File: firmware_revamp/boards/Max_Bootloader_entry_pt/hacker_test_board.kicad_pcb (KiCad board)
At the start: 2 copper layers, 109.3 x 58.3 mm, 19 parts, among them U101 TPS560430YF

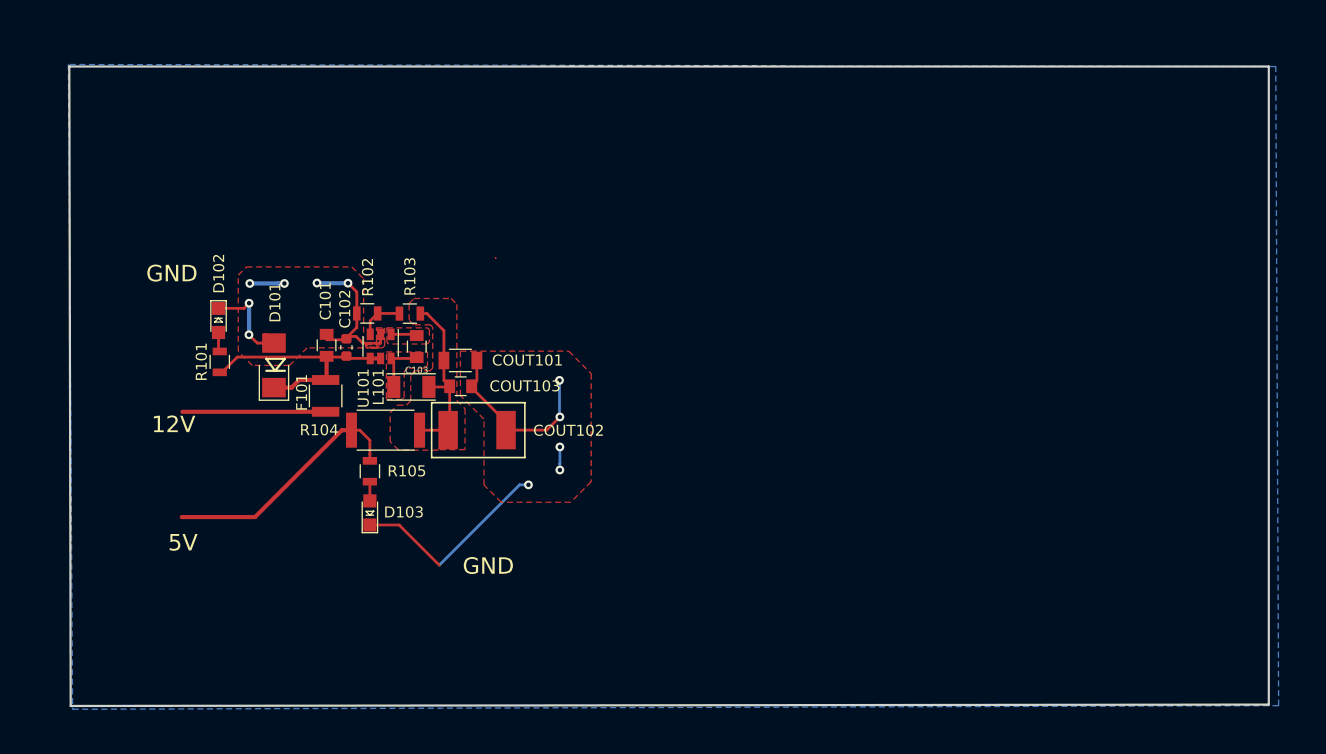
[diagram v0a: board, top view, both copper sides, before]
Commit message: Completed first layout draft of Bootloader board
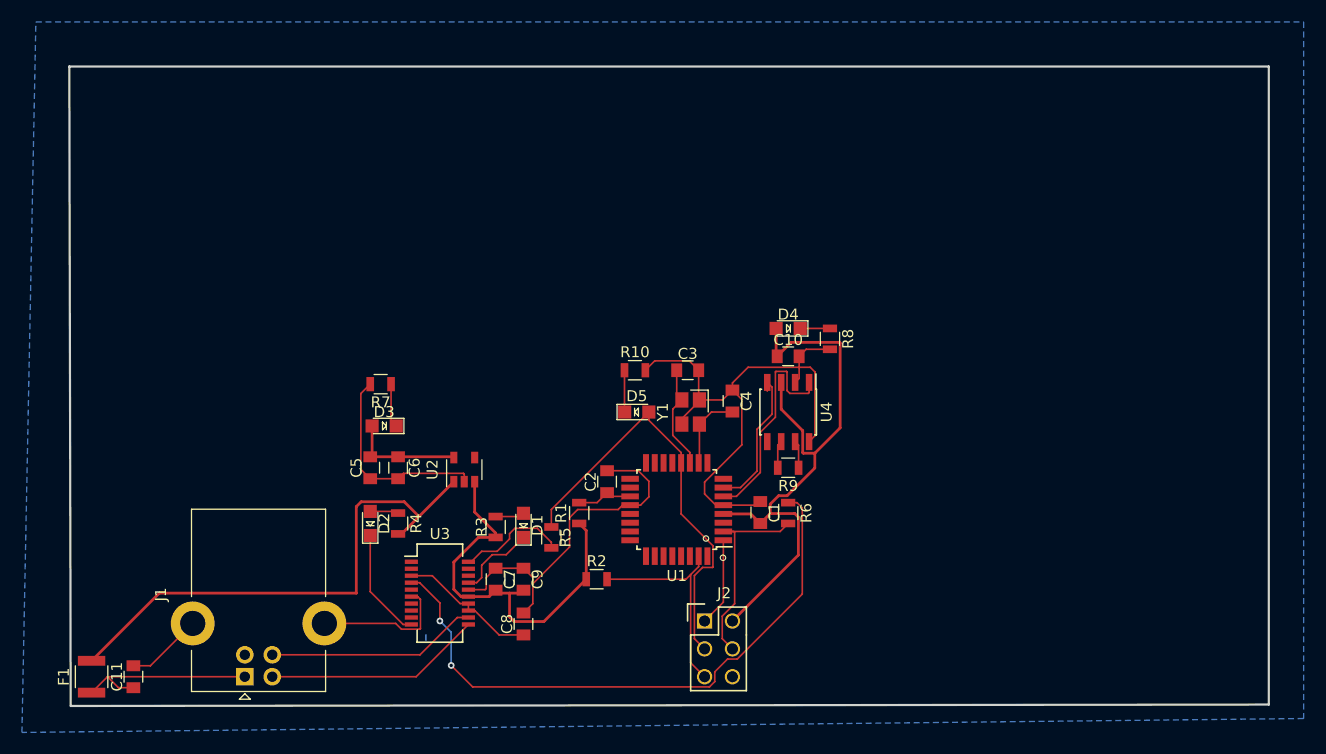
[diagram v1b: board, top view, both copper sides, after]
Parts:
- removed C101, C103: C_0.1uF, footprints:C_0805_OEM
- removed C102: C_2.2uF, footprints:C_0603_1608Metric
- removed COUT101: C_22uF, footprints:C_1206_OEM
- removed COUT102: C_33uF, footprints:Fuse_1812
- removed COUT103: C_47uF, footprints:C_0805_OEM
- removed D101: D_Zener_18V, footprints:DO-214AA
- removed D102, D103: LED_0805, footprints:LED_0805_OEM
- removed F101: F_500mA_16V, footprints:Fuse_1210
- removed L101: L_100uH, footprints:L_100uH_OEM
- removed R101: R_1K, footprints:R_0805_OEM
- removed R102: R_25K, footprints:R_0805_OEM
- removed R103: R_100K, footprints:R_0805_OEM
- removed R104: R_0_2512, footprints:R_2512_OEM
- removed R105: R_200, footprints:R_0805_OEM
- removed U101: TPS560430YF, footprints:SOT-23-6_OEM
- added C1: C_0.1uF, footprints:C_0805_OEM, F.Cu at (161.3, 117.1)
- added C10: C_0.1uF, footprints:C_0805_OEM, F.Cu at (163.8, 102.9)
- added C11: C_0.1uF, footprints:C_0805_OEM, F.Cu at (104.1, 132.1)
- added C2: C_100pF, footprints:C_0805_OEM, F.Cu at (147.3, 114.3)
- added C3: C_30pF, footprints:C_0805_OEM, F.Cu at (154.7, 104.1)
- added C4: C_30pF, footprints:C_0805_OEM, F.Cu at (158.8, 107.0)
- added C5: C_10uF, footprints:C_0805_OEM, F.Cu at (125.7, 113.0)
- added C6: C_0.1uF, footprints:C_0805_OEM, F.Cu at (128.3, 113.0)
- added C7: C_0.1uF, footprints:C_0805_OEM, F.Cu at (137.2, 123.2)
- added C8: C_0.1uF, footprints:C_0805_OEM, F.Cu at (139.7, 127.3)
- added C9: C_10uF, footprints:C_0805_OEM, F.Cu at (139.7, 123.2)
- added D1: Rx_LED, footprints:LED_0805_OEM, F.Cu at (139.7, 118.3)
- added D2: Tx_LED, footprints:LED_0805_OEM, F.Cu at (125.7, 118.1)
- added D3: 3V3_LED, footprints:LED_0805_OEM, F.Cu at (127.0, 109.2)
- added D4: 5V_LED, footprints:LED_0805_OEM, F.Cu at (163.8, 100.3)
- added D5: SCK_LED, footprints:LED_0805_OEM, F.Cu at (150.0, 108.0)
- added F1: F_500mA_16V, footprints:Fuse_1210, F.Cu at (100.3, 132.1)
- added J1: USB_B, Connector_USB:USB_B_Lumberg_2411_02_Horizontal, F.Cu at (114.3, 132.1)
- added J2: CONN_02X03, footprints:Pin_Header_Straight_2x03, F.Cu at (156.2, 127.0)
- added R1: R_100, footprints:R_0805_OEM, F.Cu at (144.8, 117.2)
- added R10: R_1K, footprints:R_0805_OEM, F.Cu at (149.9, 104.1)
- added R2: R_10K, footprints:R_0805_OEM, F.Cu at (146.4, 123.2)
- added R3: R_1K, footprints:R_0805_OEM, F.Cu at (137.2, 118.4)
- added R4: R_1K, footprints:R_0805_OEM, F.Cu at (128.3, 118.1)
- added R5: R_1K, footprints:R_0805_OEM, F.Cu at (142.2, 119.4)
- added R6: R_1K, footprints:R_0805_OEM, F.Cu at (163.8, 117.2)
- added R7: R_1K, footprints:R_0805_OEM, F.Cu at (126.7, 105.4)
- added R8: R_1K, footprints:R_0805_OEM, F.Cu at (167.6, 101.3)
- added R9: R_120_DNP, footprints:R_0805_OEM, F.Cu at (163.8, 113.0)
- added U1: ATMEGA16M1, footprints:TQFP-32_7x7mm_Pitch0.8mm, F.Cu at (153.7, 116.8)
- added U2: MIC5205-3.3YM5, Package_TO_SOT_SMD:SOT-23-5, F.Cu at (134.3, 113.2)
- added U3: FT231XS, Package_SO:SSOP-20_3.9x8.7mm_P0.635mm, F.Cu at (132.1, 124.5)
- added U4: MCP2561-E_SN, footprints:SOIC-8_3.9x4.9mm_Pitch1.27mm_OEM, F.Cu at (163.8, 108.0)
- added Y1: Crystal_SMD, footprints:Crystal_SMD_FA238, F.Cu at (154.9, 108.0)
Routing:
- net +5V: track 0.00 -> 140.8 mm
- net GND: track 65.5 -> 123.5 mm, vias 11 -> 0
- net Net-(R6-Pad1): track 0.00 -> 56.2 mm, vias 0 -> 2
- net /SCK: track 0.00 -> 39.8 mm
- net Net-(C101-Pad1): track 22.9 -> 0.00 mm
- net VCC: track 22.7 -> 0.00 mm
- net /CAN_TX: track 0.00 -> 21.3 mm
- net /USBD+: track 0.00 -> 19.9 mm
- net /RESET: track 0.00 -> 19.6 mm
- net /USBD-: track 0.00 -> 19.3 mm
- net /MOSI: track 0.00 -> 18.6 mm
- net Net-(C11-Pad1): track 0.00 -> 17.3 mm
- net Net-(COUT101-Pad1): track 17.3 -> 0.00 mm
- net /CAN_RX: track 0.00 -> 14.0 mm
- net /12V: track 13.1 -> 0.00 mm
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- removed copper zone on F.Cu, net GND
- removed copper zone on F.Cu, net Net-(C103-Pad1)
- removed copper zone on F.Cu, net Net-(C103-Pad2)
- removed copper zone on F.Cu, net Net-(COUT101-Pad1)
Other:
- board text removed: "12V"
- board text removed: "5V"
- board text removed: "GND"
